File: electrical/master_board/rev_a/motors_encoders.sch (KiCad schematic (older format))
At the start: 14 parts, among them CN3 LIDAR_ADAPTER;2xF1x2, CN55 HR2_EncoderMate;2XF1X3, CN56 HR2_EncoderMate;2XF1X3, U1 DRV8833PWPR;16HTSSOP

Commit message: Lot's schematic work.
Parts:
- removed CN3: LIDAR_ADAPTER;2xF1x2, HR2:LIDAR_ADAPTER_2xF1x2, symbol HR2:LIDAR_ADAPTER;2xF1x2
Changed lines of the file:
@@
 $Descr A4 11693 8268
 encoding utf-8
-Sheet 4 9
+Sheet 9 9
 Title "HR2 Motors and Encoders"
 Date "2020-10-03"
@@
 Text Label 8050 5000 0    50   ~ 0
 GND
-$Comp
-L HR2:LIDAR_ADAPTER;2xF1x2 CN3
-U 1 1 5F613DD3
-P 6300 5400
-F 0 "CN3" H 6550 5550 50  0000 C CNN
-F 1 "LIDAR_ADAPTER;2xF1x2" H 6800 4500 50  0000 C CNN
-F 2 "HR2:LIDAR_ADAPTER_2xF1x2" H 6500 5450 60  0001 L CNN
-F 3 "Lidar Adapter Connectors" H 6500 5250 60  0001 L CNN
-F 4 "Lidar Adapter Connectors" H 6500 5350 60  0001 L CNN "manf#"
-	1    6300 5400
-	1    0    0    -1
-$EndComp
-Text HLabel 8500 5400 2    50   Input ~ 0
-5v
-Wire Wire Line
-	7300 5700 7600 5700
-Wire Wire Line
-	7600 5700 7600 5000
-Wire Wire Line
-	7300 5400 8500 5400
-Text HLabel 8500 5500 2    50   Output ~ 0
-LDR_TX
-Text HLabel 8500 5600 2    50   Input ~ 0
-LDR_RX
-Text HLabel 8500 5800 2    50   Input ~ 0
-LDR_SPIN
-Text HLabel 8500 5900 2    50   Input ~ 0
-LDR_EN
-Text HLabel 8500 6000 2    50   Input ~ 0
-LDR_PWM
-Wire Wire Line
-	7300 6000 8500 6000
-Wire Wire Line
-	7300 5900 8500 5900
-Wire Wire Line
-	7300 5800 8500 5800
-Wire Wire Line
-	7300 5600 8500 5600
-Wire Wire Line
-	7300 5500 8500 5500
 $EndSCHEMATC

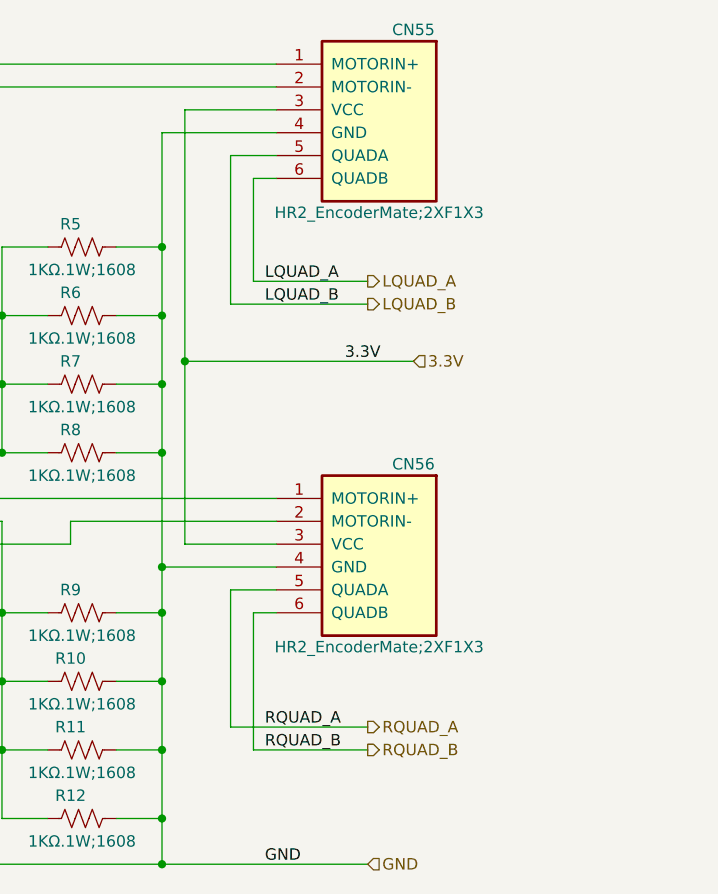
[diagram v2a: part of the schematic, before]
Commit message: Bound signals to Morpho pins.
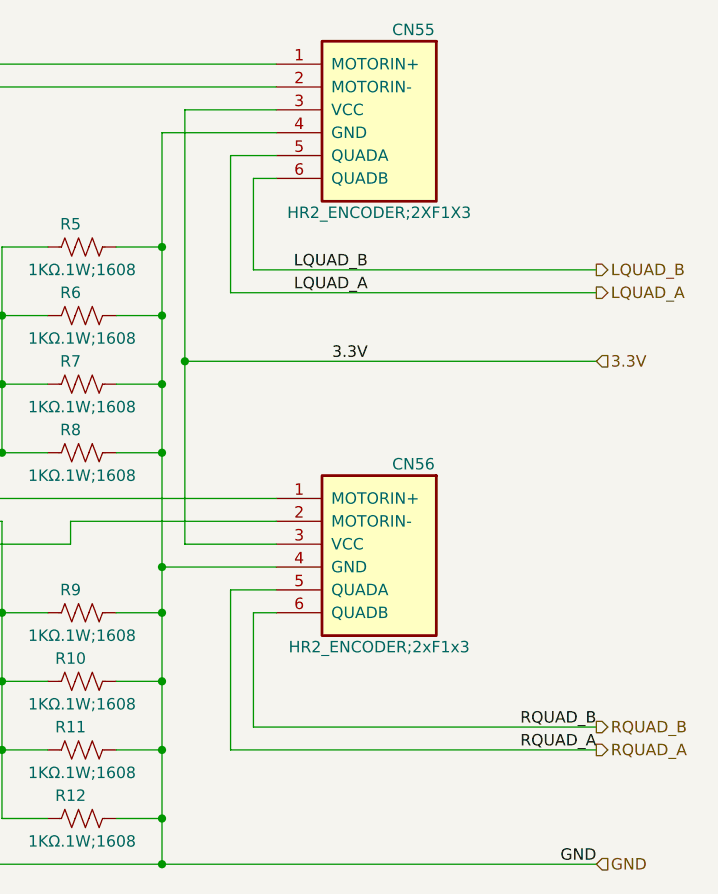
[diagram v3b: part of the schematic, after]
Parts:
- CN55: value HR2_EncoderMate;2XF1X3 -> HR2_ENCODER;2XF1X3
- CN56: value HR2_EncoderMate;2XF1X3 -> HR2_ENCODER;2xF1x3
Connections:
- net LQUAD_A: now also CN55.5 (QUADA); no longer CN55.6 (QUADB)
- net LQUAD_B: now also CN55.6 (QUADB); no longer CN55.5 (QUADA)
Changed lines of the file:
@@
 $Descr A4 11693 8268
 encoding utf-8
-Sheet 9 10
+Sheet 5 10
 Title "HR2 Motors and Encoders"
 Date "2020-10-17"
@@
 P 9000 1500
 F 0 "CN55" H 9300 1650 50  0000 C CNN
-F 1 "HR2_EncoderMate;2XF1X3" H 9450 850 50  0000 C CNN
+F 1 "HR2_ENCODER;2XF1X3" H 9450 850 50  0000 C CNN
 F 2 "HR2:ENCODER_MATE" H 9200 1550 60  0001 L CNN
 F 3 "HR2 Encoder Mating Connector" H 9200 1350 60  0001 L CNN
@@
 AR Path="/5F4A826A/5F4A92D6" Ref="CN56"  Part="1"
 F 0 "CN56" H 9300 3550 50  0000 C CNN
-F 1 "HR2_EncoderMate;2XF1X3" H 9450 2750 50  0000 C CNN
+F 1 "HR2_ENCODER;2xF1x3" H 9450 2750 50  0000 C CNN
 F 2 "HR2:ENCODER_MATE" H 9200 3450 60  0001 L CNN
 F 3 "HR2 Encoder Mating Connector" H 9200 3250 60  0001 L CNN
@@
 Wire Wire Line
 	4400 3400 8100 3400
-Text HLabel 8700 2800 2    50   Input ~ 0
+Text HLabel 9500 2800 2    50   Input ~ 0
 3.3V
-Text HLabel 8500 2550 2    50   Output ~ 0
+Text HLabel 9500 2400 2    50   Output ~ 0
 LQUAD_B
-Text HLabel 8500 2450 2    50   Output ~ 0
+Text HLabel 9500 2500 2    50   Output ~ 0
 LQUAD_A
-Text HLabel 8500 4400 2    50   Output ~ 0
+Text HLabel 9500 4500 2    50   Output ~ 0
 RQUAD_A
-Text HLabel 8500 4500 2    50   Output ~ 0
+Text HLabel 9500 4400 2    50   Output ~ 0
 RQUAD_B
 Wire Wire Line
@@
 	7600 1800 7600 2300
 Connection ~ 7600 2300
-Text HLabel 8500 5000 2    50   Input ~ 0
+Text HLabel 9500 5000 2    50   Input ~ 0
 GND
 Wire Wire Line
-	7600 5000 8500 5000
+	7600 5000 9500 5000
 Connection ~ 7600 5000
 Wire Wire Line
@@
 	7700 1700 8100 1700
 Wire Wire Line
-	8700 2800 7700 2800
+	9500 2800 7700 2800
 Connection ~ 7700 2800
 Wire Wire Line
@@
 	8100 1900 7900 1900
 Wire Wire Line
-	7900 1900 7900 2550
-Wire Wire Line
-	7900 2550 8500 2550
+	7900 1900 7900 2500
+Wire Wire Line
+	7900 2500 9500 2500
 Wire Wire Line
 	8100 2000 8000 2000
 Wire Wire Line
-	8000 2000 8000 2450
-Wire Wire Line
-	8000 2450 8500 2450
+	8000 2000 8000 2400
+Wire Wire Line
+	8000 2400 9500 2400
 Wire Wire Line
 	8100 3800 7900 3800
 Wire Wire Line
-	8500 4400 7900 4400
-Wire Wire Line
-	7900 3800 7900 4400
-Wire Wire Line
-	8500 4500 8000 4500
-Wire Wire Line
-	8000 4500 8000 3900
+	9500 4500 7900 4500
+Wire Wire Line
+	7900 3800 7900 4500
+Wire Wire Line
+	9500 4400 8000 4400
+Wire Wire Line
+	8000 4400 8000 3900
 Wire Wire Line
 	8000 3900 8100 3900
-Text Label 8400 2800 0    50   ~ 0
+Text Label 8500 2800 2    50   ~ 0
 3.3V
-Text Label 8050 4400 0    50   ~ 0
+Text Label 9500 4500 2    50   ~ 0
 RQUAD_A
-Text Label 8050 4500 0    50   ~ 0
+Text Label 9500 4400 2    50   ~ 0
 RQUAD_B
-Text Label 8050 2450 0    50   ~ 0
+Text Label 8500 2500 2    50   ~ 0
 LQUAD_A
-Text Label 8050 2550 0    50   ~ 0
+Text Label 8500 2400 2    50   ~ 0
 LQUAD_B
 Text Label 4900 4100 0    50   ~ 0
 9V
-Text Label 8050 5000 0    50   ~ 0
+Text Label 9500 5000 2    50   ~ 0
 GND
 $EndSCHEMATC

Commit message: Schematic is basically complete.
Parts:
- added C22: 10pF;1608, symbol Device:C
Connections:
- net labels added: ~MOTOR_FAULT, ~MOTOR_SLEEP
- net labels removed: MOTOR_FAULT, MOTOR_SLEEP
- wire segments 85 -> 89
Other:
- note added: "250Ω .4W Current Sense"
- note added: "Left Motor/Encoder\nConnectors"
- note added: "Motor Controller\n"
- note added: "Right Motor/Encoder\nConnectors"
- moved on the sheet: C2, C3, CN55, CN56, R10, R11, R12, R5, R6, R7, R8, R9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

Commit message: Fixed corruption of order1.lib file.
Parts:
- removed CN55: HR2_ENCODER;2XF1X3, HR2:ENCODER_MATE, symbol HR2:HR2_EncoderMate;2XF1X3
- removed CN56: HR2_ENCODER;2xF1x3, HR2:ENCODER_MATE, symbol HR2:HR2_EncoderMate;2XF1X3
- added CN55, CN56: HR2_ENCODER;2xF1x3, HR2:ENCODER_2xF1x3, symbol HR2:ENCODER;2xF1x3
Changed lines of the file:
@@
 Comment4 ""
 $EndDescr
-$Comp
-L HR2:HR2_EncoderMate;2XF1X3 CN55
-U 1 1 5F4A855F
-P 7800 2000
-F 0 "CN55" H 8100 2150 50  0000 C CNN
-F 1 "HR2_ENCODER;2XF1X3" H 8250 1350 50  0000 C CNN
-F 2 "HR2:ENCODER_MATE" H 8000 2050 60  0001 L CNN
-F 3 "HR2 Encoder Mating Connector" H 8000 1850 60  0001 L CNN
-F 4 "HR2 Encoder Mating Connector" H 8000 1750 60  0001 L CNN "Field5"
-	1    7800 2000
-	-1   0    0    -1
-$EndComp
-$Comp
-L HR2:HR2_EncoderMate;2XF1X3 CN?
-U 1 1 5F4A92D6
-P 7800 3900
-AR Path="/5F4A92D6" Ref="CN?"  Part="1"
-AR Path="/5F4A826A/5F4A92D6" Ref="CN56"  Part="1"
-F 0 "CN56" H 8100 4050 50  0000 C CNN
-F 1 "HR2_ENCODER;2xF1x3" H 8250 3250 50  0000 C CNN
-F 2 "HR2:ENCODER_MATE" H 8000 3950 60  0001 L CNN
-F 3 "HR2 Encoder Mating Connector" H 8000 3750 60  0001 L CNN
-F 4 "HR2 Encoder Mating Connector" H 8000 3650 60  0001 L CNN "Field5"
-	1    7800 3900
-	-1   0    0    -1
-$EndComp
 Wire Wire Line
 	3300 5100 3300 4700
@@
 U 1 1 5FA19E5E
 P 3900 5250
-F 0 "C22" H 3800 5350 50  0000 L CNN
+F 0 "C22" H 3750 5350 50  0000 L CNN
 F 1 "10pF;1608" H 3500 5150 50  0000 L CNN
 F 2 "" H 3938 5100 50  0001 C CNN
@@
 Wire Wire Line
 	3900 5500 4800 5500
+$Comp
+L HR2:ENCODER;2xF1x3 CN55
+U 1 1 5F967601
+P 7800 2000
+F 0 "CN55" H 8500 2150 50  0000 R CNN
+F 1 "HR2_ENCODER;2xF1x3" H 8650 1350 50  0000 R CNN
+F 2 "HR2:ENCODER_2xF1x3" H 8000 2050 60  0001 L CNN
+F 3 "HR2 Encoder Connectors" H 8000 1850 60  0001 L CNN
+F 4 "HR2 Encoder Connector" H 8000 1750 60  0001 L CNN "Field5"
+	1    7800 2000
+	-1   0    0    -1
+$EndComp
+$Comp
+L HR2:ENCODER;2xF1x3 CN56
+U 1 1 5F968E59
+P 7800 3900
+F 0 "CN56" H 8500 4050 50  0000 R CNN
+F 1 "HR2_ENCODER;2xF1x3" H 8650 3250 50  0000 R CNN
+F 2 "HR2:ENCODER_2xF1x3" H 8000 3950 60  0001 L CNN
+F 3 "HR2 Encoder Connectors" H 8000 3750 60  0001 L CNN
+F 4 "HR2 Encoder Connector" H 8000 3650 60  0001 L CNN "Field5"
+	1    7800 3900
+	-1   0    0    -1
+$EndComp
 $EndSCHEMATC

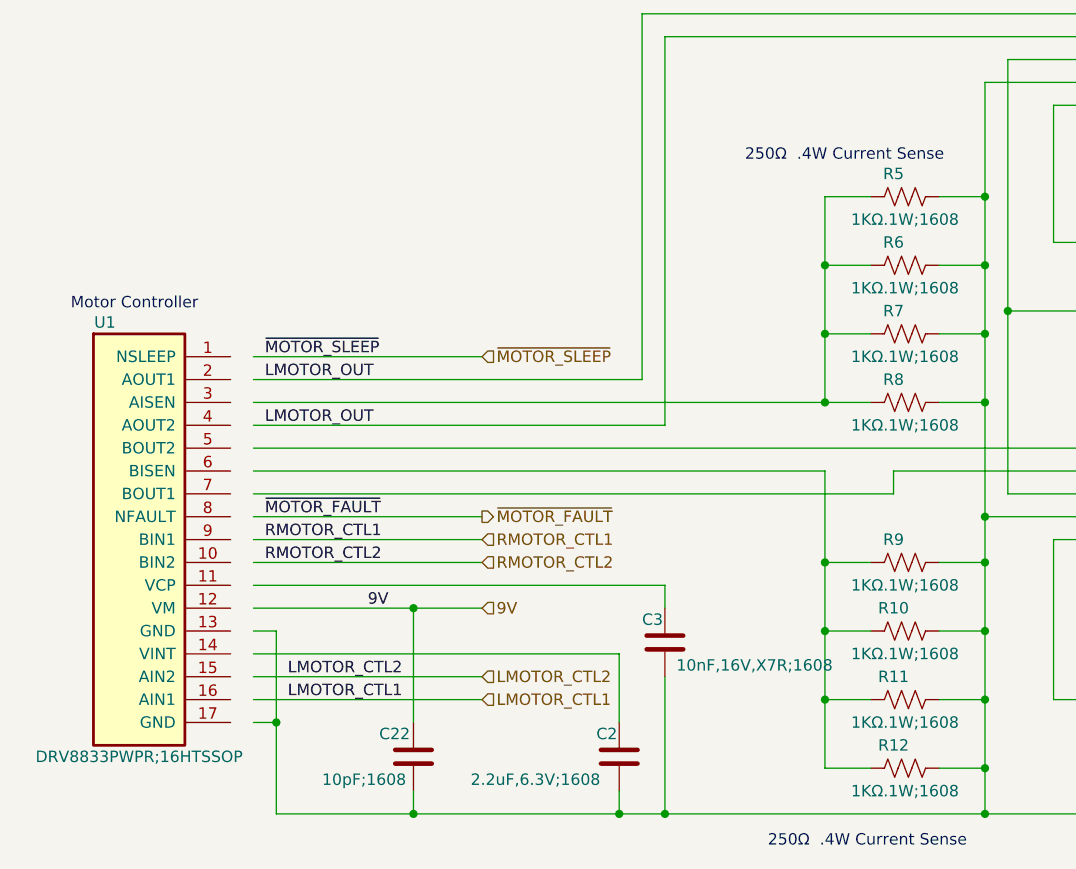
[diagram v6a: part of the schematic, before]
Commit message: Reannoted. Postioned components are in the 80-99 reference range.
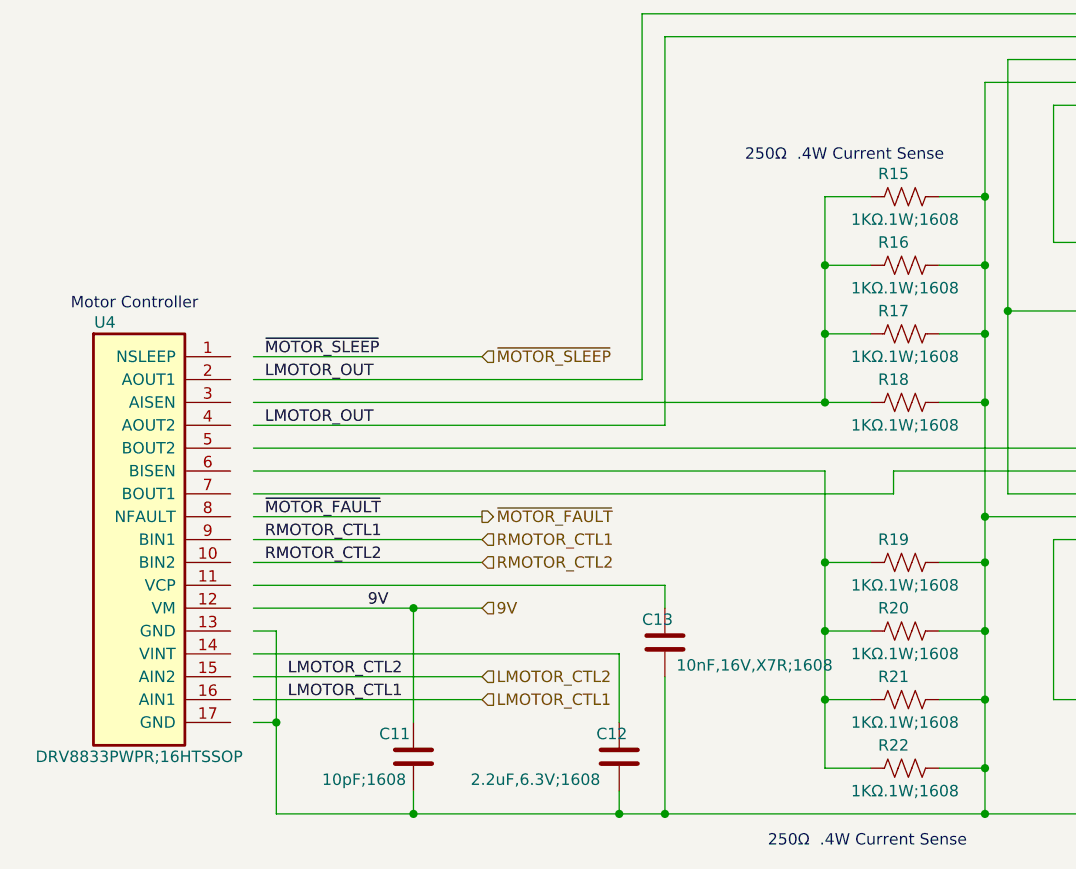
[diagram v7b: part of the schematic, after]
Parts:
- renumbered C22 to C11, C2 to C12, C3 to C13, CN56 to CN91, CN55 to CN92, R5 to R15, R6 to R16, R7 to R17, R8 to R18, R9 to R19, R10 to R20, R11 to R21, R12 to R22, U1 to U4
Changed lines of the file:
@@
 LMOTOR_CTL1
 $Comp
-L HR2:DRV8833PWPR;16HTSSOP U1
+L HR2:DRV8833PWPR;16HTSSOP U4
 U 1 1 5F4C0C8C
 P 2300 3500
-F 0 "U1" H 2550 3650 50  0000 C CNN
+F 0 "U4" H 2550 3650 50  0000 C CNN
 F 1 "DRV8833PWPR;16HTSSOP" H 2700 1750 50  0000 C CNN
 F 2 "Package_SO:HTSSOP-16-1EP_4.4x5mm_P0.65mm_EP3.4x5mm_Mask3x3mm_ThermalVias" H 2500 3550 60  0001 L CNN
@@
 	5000 4500 5000 4600
 $Comp
-L Device:C C3
+L Device:C C13
 U 1 1 5F4C3DE1
 P 5000 4750
-F 0 "C3" H 4900 4850 50  0000 L CNN
+F 0 "C13" H 4900 4850 50  0000 L CNN
 F 1 "10nF,16V,X7R;1608" H 5050 4650 50  0000 L CNN
 F 2 "" H 5038 4600 50  0001 C CNN
@@
 $EndComp
 $Comp
-L Device:C C2
+L Device:C C12
 U 1 1 5F4CB112
 P 4800 5250
-F 0 "C2" H 4700 5350 50  0000 L CNN
+F 0 "C12" H 4700 5350 50  0000 L CNN
 F 1 "2.2uF,6.3V;1608" H 4150 5150 50  0000 L CNN
 F 2 "" H 4838 5100 50  0001 C CNN
@@
 Connection ~ 4800 5500
 $Comp
-L Device:R_US R12
+L Device:R_US R22
 U 1 1 5F4D52D3
 P 6050 5300
-F 0 "R12" V 5950 5250 50  0000 C CNN
+F 0 "R22" V 5950 5250 50  0000 C CNN
 F 1 "1KΩ.1W;1608" V 6150 5300 50  0000 C CNN
 F 2 "" V 6090 5290 50  0001 C CNN
@@
 $EndComp
 $Comp
-L Device:R_US R11
+L Device:R_US R21
 U 1 1 5F4D52DD
 P 6050 5000
-F 0 "R11" V 5950 4950 50  0000 C CNN
+F 0 "R21" V 5950 4950 50  0000 C CNN
 F 1 "1KΩ.1W;1608" V 6150 5000 50  0000 C CNN
 F 2 "" V 6090 4990 50  0001 C CNN
@@
 $EndComp
 $Comp
-L Device:R_US R10
+L Device:R_US R20
 U 1 1 5F4D52E7
 P 6050 4700
-F 0 "R10" V 5950 4650 50  0000 C CNN
+F 0 "R20" V 5950 4650 50  0000 C CNN
 F 1 "1KΩ.1W;1608" V 6150 4700 50  0000 C CNN
 F 2 "" V 6090 4690 50  0001 C CNN
@@
 $EndComp
 $Comp
-L Device:R_US R9
+L Device:R_US R19
 U 1 1 5F4D52F1
 P 6050 4400
-F 0 "R9" V 5950 4350 50  0000 C CNN
+F 0 "R19" V 5950 4350 50  0000 C CNN
 F 1 "1KΩ.1W;1608" V 6150 4400 50  0000 C CNN
 F 2 "" V 6090 4390 50  0001 C CNN
@@
 	6200 3700 6400 3700
 $Comp
-L Device:R_US R5
+L Device:R_US R15
 U 1 1 5F4CD3C4
 P 6050 2800
-F 0 "R5" V 5950 2750 50  0000 C CNN
+F 0 "R15" V 5950 2750 50  0000 C CNN
 F 1 "1KΩ.1W;1608" V 6150 2800 50  0000 C CNN
 F 2 "" V 6090 2790 50  0001 C CNN
@@
 $EndComp
 $Comp
-L Device:R_US R6
+L Device:R_US R16
 U 1 1 5F4CCE9C
 P 6050 3100
-F 0 "R6" V 5950 3050 50  0000 C CNN
+F 0 "R16" V 5950 3050 50  0000 C CNN
 F 1 "1KΩ.1W;1608" V 6150 3100 50  0000 C CNN
 F 2 "" V 6090 3090 50  0001 C CNN
@@
 $EndComp
 $Comp
-L Device:R_US R7
+L Device:R_US R17
 U 1 1 5F4CC9D3
 P 6050 3400
-F 0 "R7" V 5950 3350 50  0000 C CNN
+F 0 "R17" V 5950 3350 50  0000 C CNN
 F 1 "1KΩ.1W;1608" V 6150 3400 50  0000 C CNN
 F 2 "" V 6090 3390 50  0001 C CNN
@@
 $EndComp
 $Comp
-L Device:R_US R8
+L Device:R_US R18
 U 1 1 5F4CC3F2
 P 6050 3700
-F 0 "R8" V 5950 3650 50  0000 C CNN
+F 0 "R18" V 5950 3650 50  0000 C CNN
 F 1 "1KΩ.1W;1608" V 6150 3700 50  0000 C CNN
 F 2 "" V 6090 3690 50  0001 C CNN
@@
 Left Motor/Encoder\nConnectors
 $Comp
-L Device:C C22
+L Device:C C11
 U 1 1 5FA19E5E
 P 3900 5250
-F 0 "C22" H 3750 5350 50  0000 L CNN
+F 0 "C11" H 3750 5350 50  0000 L CNN
 F 1 "10pF;1608" H 3500 5150 50  0000 L CNN
 F 2 "" H 3938 5100 50  0001 C CNN
@@
 	3900 5500 4800 5500
 $Comp
-L HR2:ENCODER;2xF1x3 CN55
+L HR2:ENCODER;2xF1x3 CN92
 U 1 1 5F967601
 P 7800 2000
-F 0 "CN55" H 8500 2150 50  0000 R CNN
+F 0 "CN92" H 8500 2150 50  0000 R CNN
 F 1 "HR2_ENCODER;2xF1x3" H 8650 1350 50  0000 R CNN
 F 2 "HR2:ENCODER_2xF1x3" H 8000 2050 60  0001 L CNN
@@
 $EndComp
 $Comp
-L HR2:ENCODER;2xF1x3 CN56
+L HR2:ENCODER;2xF1x3 CN91
 U 1 1 5F968E59
 P 7800 3900
-F 0 "CN56" H 8500 4050 50  0000 R CNN
+F 0 "CN91" H 8500 4050 50  0000 R CNN
 F 1 "HR2_ENCODER;2xF1x3" H 8650 3250 50  0000 R CNN
 F 2 "HR2:ENCODER_2xF1x3" H 8000 3950 60  0001 L CNN

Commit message: Assigned PCB footprints.
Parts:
- C11, C12, C13: footprint (none) -> Capacitor_SMD:C_0603_1608Metric
- R15, R16, R17, R18, R19, R20, R21, R22: footprint (none) -> Resistor_SMD:R_0603_1608Metric
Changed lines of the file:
@@
 F 0 "C13" H 4900 4850 50  0000 L CNN
 F 1 "10nF,16V,X7R;1608" H 5050 4650 50  0000 L CNN
-F 2 "" H 5038 4600 50  0001 C CNN
+F 2 "Capacitor_SMD:C_0603_1608Metric" H 5038 4600 50  0001 C CNN
 F 3 "~" H 5000 4750 50  0001 C CNN
 	1    5000 4750
@@
 F 0 "C12" H 4700 5350 50  0000 L CNN
 F 1 "2.2uF,6.3V;1608" H 4150 5150 50  0000 L CNN
-F 2 "" H 4838 5100 50  0001 C CNN
+F 2 "Capacitor_SMD:C_0603_1608Metric" H 4838 5100 50  0001 C CNN
 F 3 "~" H 4800 5250 50  0001 C CNN
 	1    4800 5250
@@
 F 0 "R22" V 5950 5250 50  0000 C CNN
 F 1 "1KΩ.1W;1608" V 6150 5300 50  0000 C CNN
-F 2 "" V 6090 5290 50  0001 C CNN
+F 2 "Resistor_SMD:R_0603_1608Metric" V 6090 5290 50  0001 C CNN
 F 3 "~" H 6050 5300 50  0001 C CNN
 	1    6050 5300
@@
 F 0 "R21" V 5950 4950 50  0000 C CNN
 F 1 "1KΩ.1W;1608" V 6150 5000 50  0000 C CNN
-F 2 "" V 6090 4990 50  0001 C CNN
+F 2 "Resistor_SMD:R_0603_1608Metric" V 6090 4990 50  0001 C CNN
 F 3 "~" H 6050 5000 50  0001 C CNN
 	1    6050 5000
@@
 F 0 "R20" V 5950 4650 50  0000 C CNN
 F 1 "1KΩ.1W;1608" V 6150 4700 50  0000 C CNN
-F 2 "" V 6090 4690 50  0001 C CNN
+F 2 "Resistor_SMD:R_0603_1608Metric" V 6090 4690 50  0001 C CNN
 F 3 "~" H 6050 4700 50  0001 C CNN
 	1    6050 4700
@@
 F 0 "R19" V 5950 4350 50  0000 C CNN
 F 1 "1KΩ.1W;1608" V 6150 4400 50  0000 C CNN
-F 2 "" V 6090 4390 50  0001 C CNN
+F 2 "Resistor_SMD:R_0603_1608Metric" V 6090 4390 50  0001 C CNN
 F 3 "~" H 6050 4400 50  0001 C CNN
 	1    6050 4400
@@
 F 0 "R15" V 5950 2750 50  0000 C CNN
 F 1 "1KΩ.1W;1608" V 6150 2800 50  0000 C CNN
-F 2 "" V 6090 2790 50  0001 C CNN
+F 2 "Resistor_SMD:R_0603_1608Metric" V 6090 2790 50  0001 C CNN
 F 3 "~" H 6050 2800 50  0001 C CNN
 	1    6050 2800
@@
 F 0 "R16" V 5950 3050 50  0000 C CNN
 F 1 "1KΩ.1W;1608" V 6150 3100 50  0000 C CNN
-F 2 "" V 6090 3090 50  0001 C CNN
+F 2 "Resistor_SMD:R_0603_1608Metric" V 6090 3090 50  0001 C CNN
 F 3 "~" H 6050 3100 50  0001 C CNN
 	1    6050 3100
@@
 F 0 "R17" V 5950 3350 50  0000 C CNN
 F 1 "1KΩ.1W;1608" V 6150 3400 50  0000 C CNN
-F 2 "" V 6090 3390 50  0001 C CNN
+F 2 "Resistor_SMD:R_0603_1608Metric" V 6090 3390 50  0001 C CNN
 F 3 "~" H 6050 3400 50  0001 C CNN
 	1    6050 3400
@@
 F 0 "R18" V 5950 3650 50  0000 C CNN
 F 1 "1KΩ.1W;1608" V 6150 3700 50  0000 C CNN
-F 2 "" V 6090 3690 50  0001 C CNN
+F 2 "Resistor_SMD:R_0603_1608Metric" V 6090 3690 50  0001 C CNN
 F 3 "~" H 6050 3700 50  0001 C CNN
 	1    6050 3700
@@
 F 0 "C11" H 3750 5350 50  0000 L CNN
 F 1 "10pF;1608" H 3500 5150 50  0000 L CNN
-F 2 "" H 3938 5100 50  0001 C CNN
+F 2 "Capacitor_SMD:C_0603_1608Metric" H 3938 5100 50  0001 C CNN
 F 3 "~" H 3900 5250 50  0001 C CNN
 	1    3900 5250
